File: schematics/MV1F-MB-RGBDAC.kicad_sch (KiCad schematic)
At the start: 32 parts, among them U3 74LS245, U5 74LS245, U6 74LS32

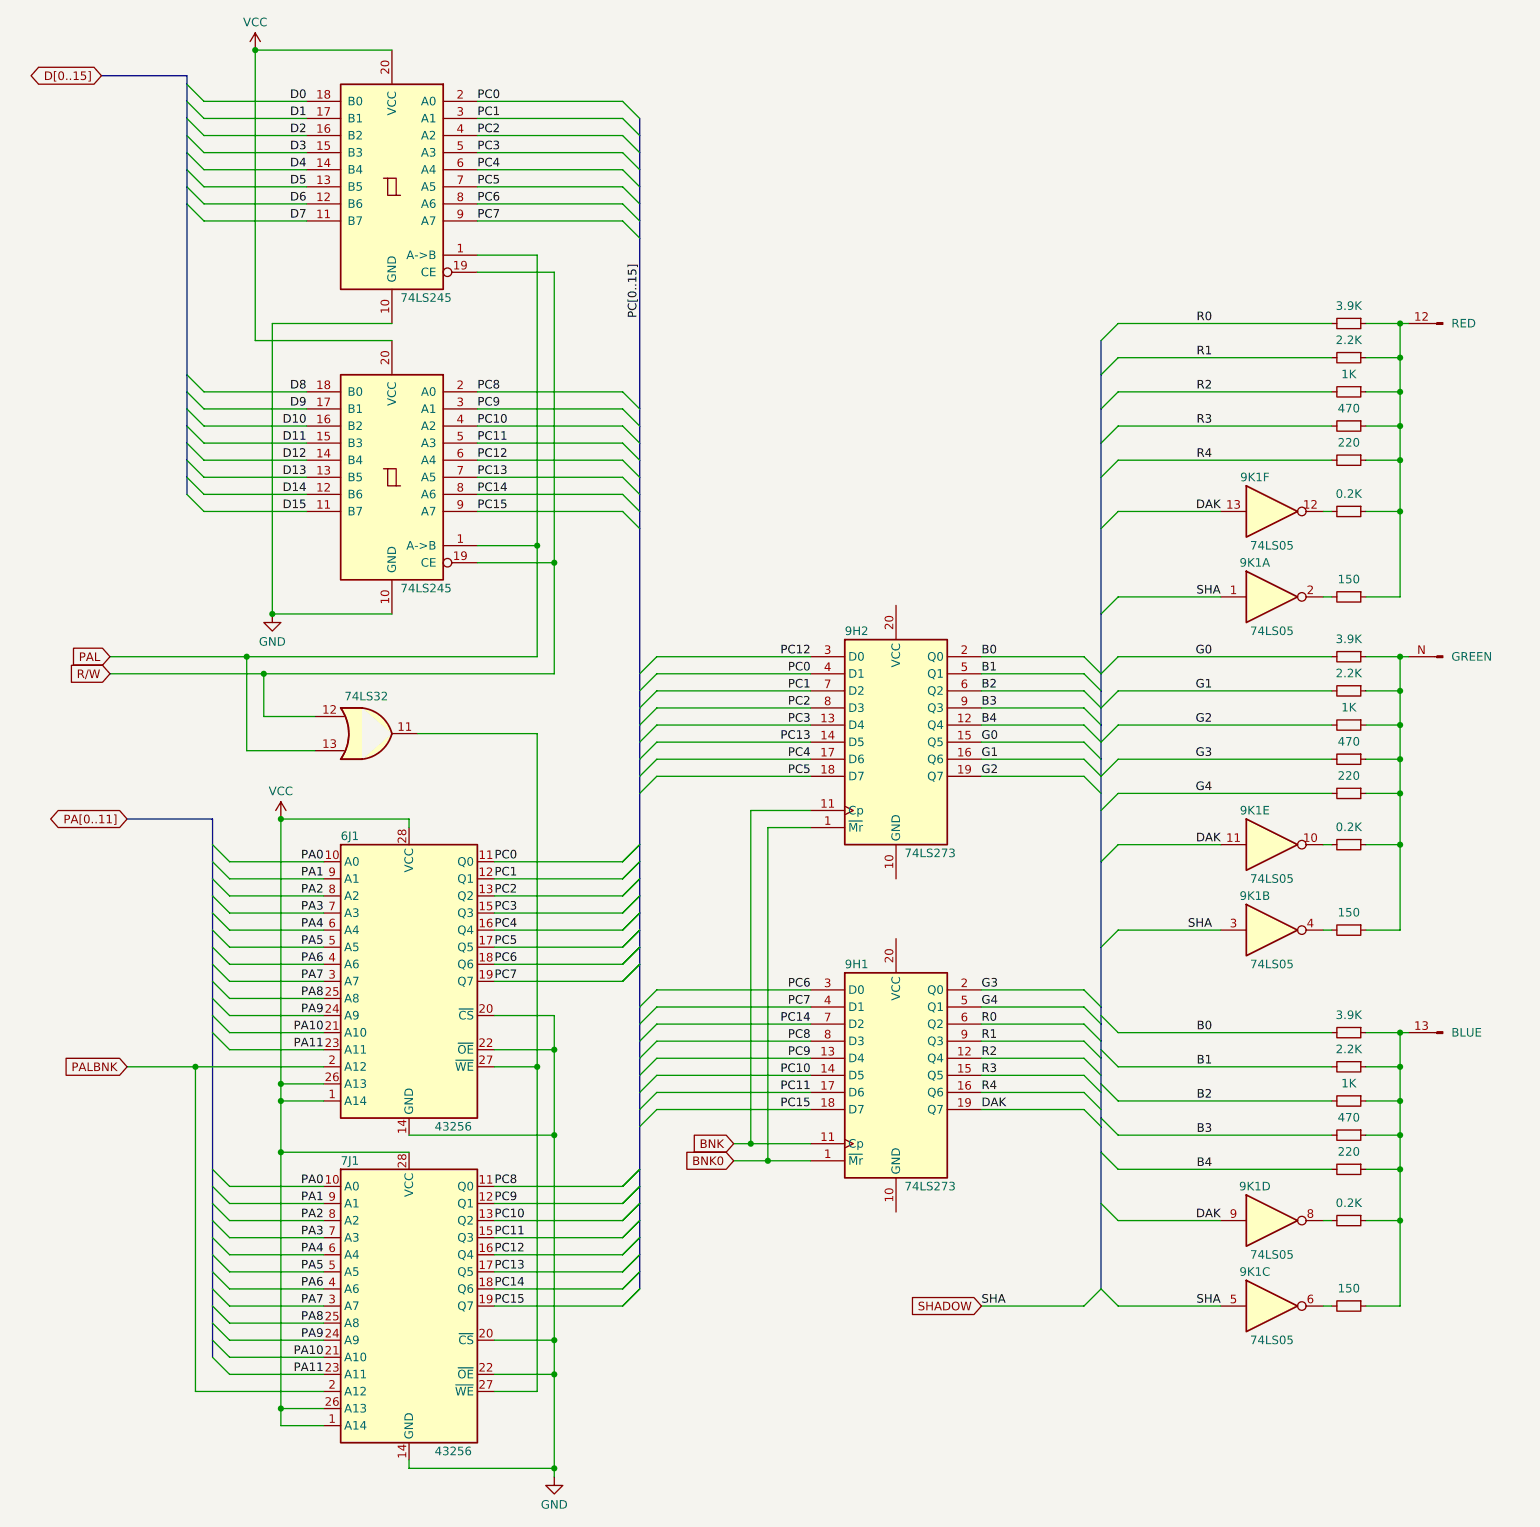
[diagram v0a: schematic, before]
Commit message: Typo... and orphan labels remove
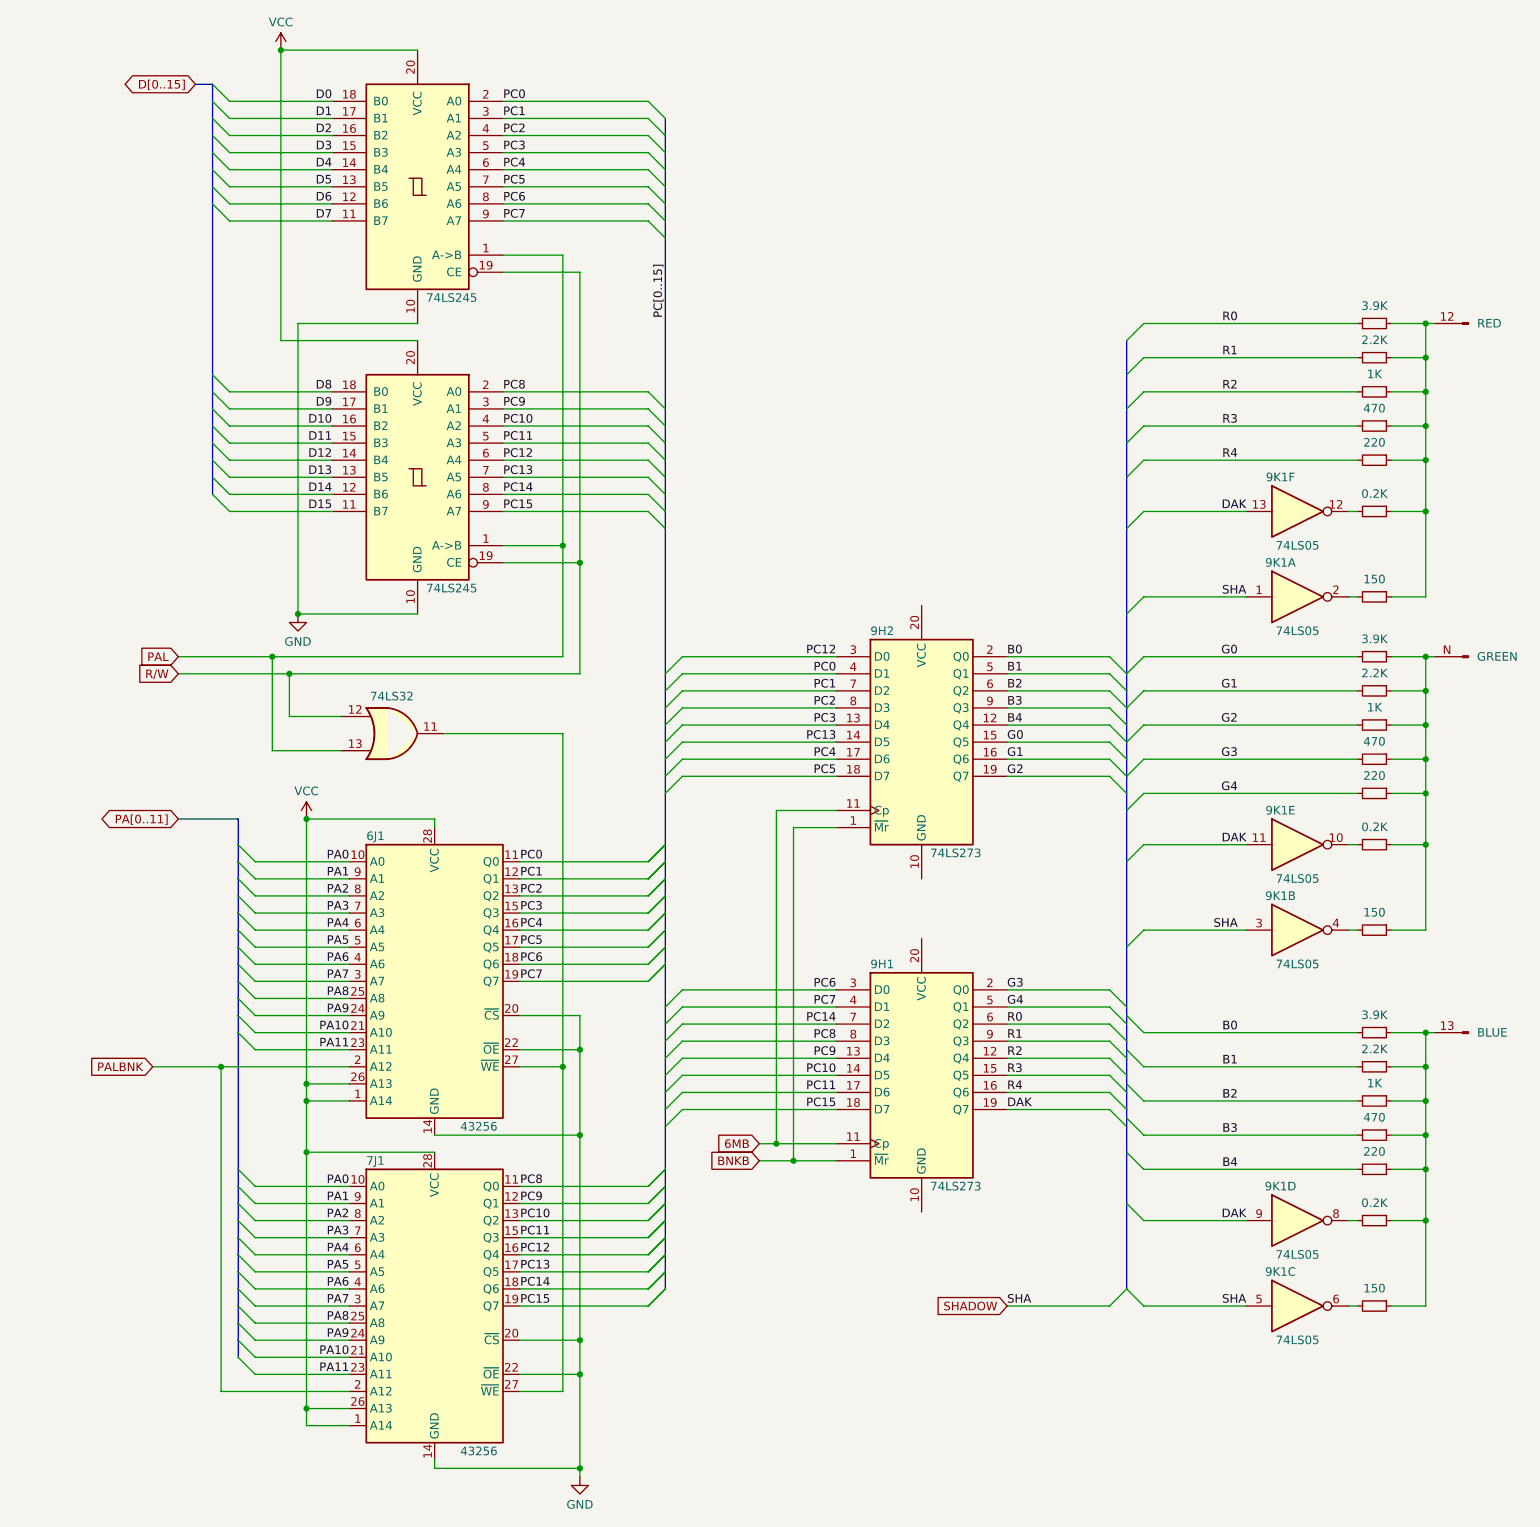
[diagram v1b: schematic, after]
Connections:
- net BNK renamed 6MB
- net BNK0 renamed BNKB
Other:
- moved on the sheet: 6J1, 7J1, 9H1, 9H2, 9K1A, 9K1B, 9K1C, 9K1D, 9K1E, 9K1F
